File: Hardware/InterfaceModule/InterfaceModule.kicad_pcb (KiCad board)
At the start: 2 copper layers, 43 parts, among them J1 Selector Knob Connector, J10 External MIC IN, J11 TS-480 DATA, J12 D-700 DATA, J13 SignaLink 2 RADIO, J14 SignaLink 1 RADIO, J15 D-700 COM, J16 TS-480 COM, J17 External COM, J2 KrakenSDR Relay Enable, J3 External GPS IN, J4 External GPS OUT, J5 D-700 GPS, J6 D-700 MIC, J7 TS-480 MIC, J8 D-700 EXT.SP 1, J9 TS-480 EXT.SP, K1 FINDER-40.52, K10 FINDER-40.52, K11 FINDER-40.52, K12 FINDER-40.52, K13 FINDER-40.52, K14 FINDER-40.52, K15 FINDER-40.52, K16 FINDER-40.52, K17 FINDER-40.52, K18 FINDER-40.52, K19 FINDER-40.52, K2 FINDER-40.52, K20 FINDER-40.52, K21 FINDER-40.52, K22 FINDER-40.52, K3 FINDER-40.52, K4 FINDER-40.52, K5 FINDER-40.52, K6 FINDER-40.52, K7 FINDER-40.52, K8 FINDER-40.52, K9 FINDER-40.52

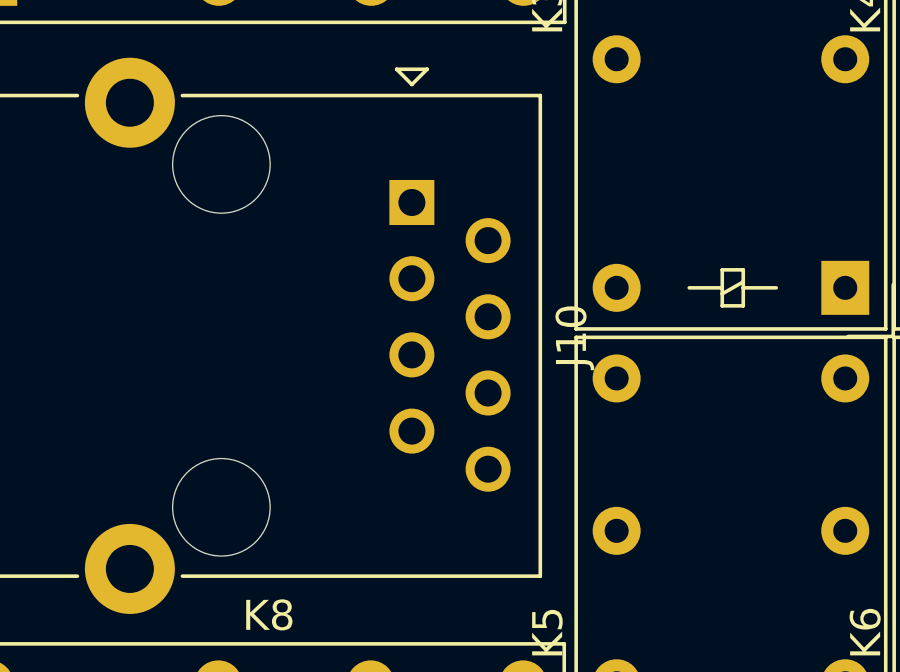
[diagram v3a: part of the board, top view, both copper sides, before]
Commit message: Added backplane between boards, redesigned selector
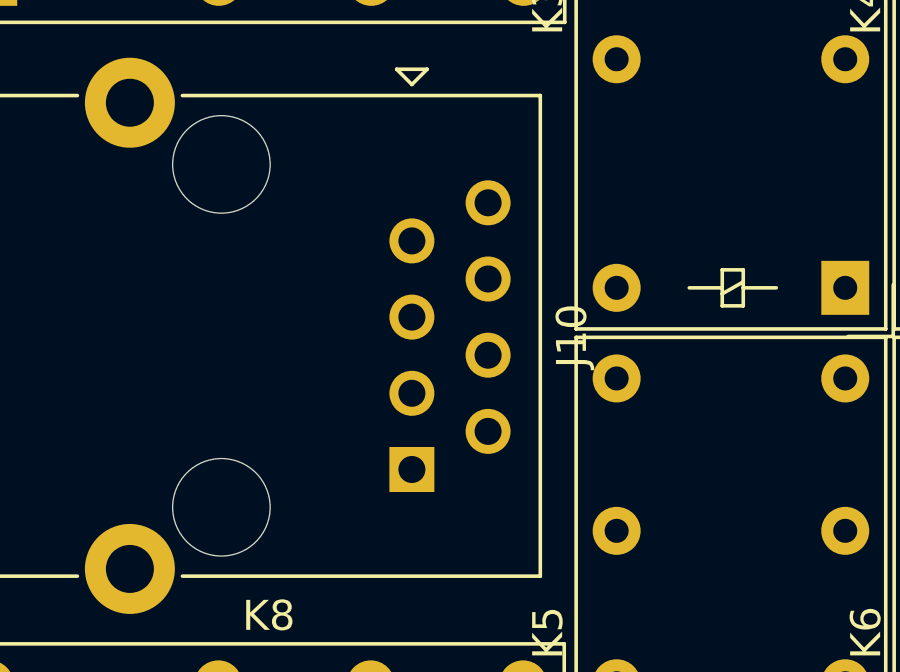
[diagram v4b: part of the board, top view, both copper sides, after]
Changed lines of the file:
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@@
     (pad "" np_thru_hole circle (at -1.27 6.35 270) (size 3.25 3.25) (drill 3.25) (layers *.Cu *.Mask))
     (pad "" np_thru_hole circle (at 10.16 6.35 90) (size 3.25 3.25) (drill 3.25) (layers *.Cu *.Mask))
-    (pad "1" thru_hole rect (at 0 0 90) (size 1.5 1.5) (drill 0.9) (layers *.Cu *.Mask)
+    (pad "1" thru_hole rect (at 8.9 0 90) (size 1.5 1.5) (drill 0.9) (layers *.Cu *.Mask)
       (net 22 "/Microphone Switching/EXT_UP") (pintype "passive"))
-    (pad "2" thru_hole circle (at 1.27 -2.54 90) (size 1.5 1.5) (drill 0.9) (layers *.Cu *.Mask)
+    (pad "2" thru_hole circle (at 7.63 -2.54 90) (size 1.5 1.5) (drill 0.9) (layers *.Cu *.Mask)
       (net 28 "/Microphone Switching/EXT_8V") (pintype "passive"))
-    (pad "3" thru_hole circle (at 2.54 0 90) (size 1.5 1.5) (drill 0.9) (layers *.Cu *.Mask)
+    (pad "3" thru_hole circle (at 6.36 0 90) (size 1.5 1.5) (drill 0.9) (layers *.Cu *.Mask)
       (net 29 "/Microphone Switching/EXT_GND") (pintype "passive"))
-    (pad "4" thru_hole circle (at 3.81 -2.54 90) (size 1.5 1.5) (drill 0.9) (layers *.Cu *.Mask)
+    (pad "4" thru_hole circle (at 5.09 -2.54 90) (size 1.5 1.5) (drill 0.9) (layers *.Cu *.Mask)
       (net 30 "/Microphone Switching/EXT_PTT") (pintype "passive"))
-    (pad "5" thru_hole circle (at 5.08 0 90) (size 1.5 1.5) (drill 0.9) (layers *.Cu *.Mask)
+    (pad "5" thru_hole circle (at 3.82 0 90) (size 1.5 1.5) (drill 0.9) (layers *.Cu *.Mask)
       (net 31 "/Microphone Switching/EXT_MICGND") (pintype "passive"))
-    (pad "6" thru_hole circle (at 6.35 -2.54 90) (size 1.5 1.5) (drill 0.9) (layers *.Cu *.Mask)
+    (pad "6" thru_hole circle (at 2.55 -2.54 90) (size 1.5 1.5) (drill 0.9) (layers *.Cu *.Mask)
       (net 33 "/Microphone Switching/EXT_MIC") (pintype "passive"))
-    (pad "7" thru_hole circle (at 7.62 0 90) (size 1.5 1.5) (drill 0.9) (layers *.Cu *.Mask)
+    (pad "7" thru_hole circle (at 1.28 0 90) (size 1.5 1.5) (drill 0.9) (layers *.Cu *.Mask)
       (net 34 "/Microphone Switching/EXT_NC") (pintype "passive"))
-    (pad "8" thru_hole circle (at 8.89 -2.54 90) (size 1.5 1.5) (drill 0.9) (layers *.Cu *.Mask)
+    (pad "8" thru_hole circle (at 0.01 -2.54 90) (size 1.5 1.5) (drill 0.9) (layers *.Cu *.Mask)
       (net 35 "/Microphone Switching/EXT_DWN") (pintype "passive"))
     (pad "SH" thru_hole circle (at -3.325 9.4 270) (size 3 3) (drill 1.6) (layers *.Cu *.Mask)

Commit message: Initial routings of data and main boards
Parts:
- removed J1: Selector Knob Connector, Connector_RJ:RJ45_Ninigi_GE
- removed J10: External MIC IN, Connector_RJ:RJ45_Ninigi_GE
- removed J11: TS-480 DATA, libraries:Connector_Mini-DIN_Female_6Pin_2rows
- removed J12: D-700 DATA, libraries:Connector_Mini-DIN_Female_6Pin_2rows
- removed J13: SignaLink 2 RADIO, Connector_RJ:RJ45_Ninigi_GE
- removed J14: SignaLink 1 RADIO, Connector_RJ:RJ45_Ninigi_GE
- removed J15: D-700 COM, Connector_Dsub:DSUB-9_Male_Horizontal_P2.77x2.84mm_EdgePinOffset7.70mm_Housed_MountingHolesOffset9.12mm
- removed J16: TS-480 COM, Connector_Dsub:DSUB-9_Male_Horizontal_P2.77x2.84mm_EdgePinOffset7.70mm_Housed_MountingHolesOffset9.12mm
- removed J17: External COM, Connector_Dsub:DSUB-9_Male_Horizontal_P2.77x2.84mm_EdgePinOffset7.70mm_Housed_MountingHolesOffset9.12mm
- removed J2: KrakenSDR Relay Enable, TerminalBlock_Phoenix:TerminalBlock_Phoenix_MKDS-1,5-2_1x02_P5.00mm_Horizontal
- removed J3: External GPS IN, Connector_Dsub:DSUB-9_Male_Horizontal_P2.77x2.84mm_EdgePinOffset7.70mm_Housed_MountingHolesOffset9.12mm
- removed J4: External GPS OUT, Connector_Dsub:DSUB-9_Male_Horizontal_P2.77x2.84mm_EdgePinOffset7.70mm_Housed_MountingHolesOffset9.12mm
- removed J5: D-700 GPS, libraries:Mystery_3.5mm
- removed J6: D-700 MIC, Connector_RJ:RJ45_Ninigi_GE
- removed J7: TS-480 MIC, Connector_RJ:RJ45_Ninigi_GE
- removed J8: D-700 EXT.SP 1, libraries:Mystery_3.5mm
- removed J9: TS-480 EXT.SP, libraries:Mystery_3.5mm
- removed K1, K10, K11, K12, K13, K14, K15, K16, K17, K18, K19, K2, K20, K21, K22, K3, K4, K5, K6, K7, K8, K9: FINDER-40.52, Relay_THT:Relay_DPDT_Finder_30.22
- removed R1, R2: 3.9Ohm, Resistor_THT:R_Axial_DIN0204_L3.6mm_D1.6mm_P2.54mm_Vertical
- removed R3, R4: 470Ohm, Resistor_THT:R_Axial_DIN0204_L3.6mm_D1.6mm_P2.54mm_Vertical
- added F101: 1A Trip, Fuse:Fuse_Bourns_MF-RG300, F.Cu at (-260.0, 69.0)
- added H101: Mounting Hole, libraries:M3_Mounting, F.Cu at (-274.0, 7.24)
- added H102: Mounting Hole, libraries:M3_Mounting, F.Cu at (-191.0, 7.24)
- added H103: Mounting Hole, libraries:M3_Mounting, F.Cu at (-191.0, 90.2)
- added H104: Mounting Hole, libraries:M3_Mounting, F.Cu at (-274.0, 90.2)
- added H201: Mounting Hole, libraries:M3_Mounting, F.Cu at (-112.0, 89.7)
- added H202: Mounting Hole, libraries:M3_Mounting, F.Cu at (-29.0, 6.74)
- added H203: Mounting Hole, libraries:M3_Mounting, F.Cu at (-112.0, 6.74)
- added H204: Mounting Hole, libraries:M3_Mounting, F.Cu at (-29.0, 89.7)
- added H301: Mounting Hole, libraries:M3_Mounting, F.Cu at (-200.0, 171.2)
- added H302: Mounting Hole, libraries:M3_Mounting, F.Cu at (-200.0, 254.2)
- added H303: Mounting Hole, libraries:M3_Mounting, F.Cu at (-283.0, 171.2)
- added H304: Mounting Hole, libraries:M3_Mounting, F.Cu at (-283.0, 254.2)
- added H401: Mounting Hole, libraries:M3_Mounting, F.Cu at (-29.0, 253.5)
- added H402: Mounting Hole, libraries:M3_Mounting, F.Cu at (-112.0, 170.5)
- added H403: Mounting Hole, libraries:M3_Mounting, F.Cu at (-112.0, 253.5)
- added H404: Mounting Hole, libraries:M3_Mounting, F.Cu at (-29.0, 170.5)
- added J101: Out 1 Header Debug Holes, libraries:2x07_Debug_Holes, F.Cu at (-255.3, 27.3)
- added J102: 2x05 IDC Header - OUT 1, Connector_IDC:IDC-Header_2x05_P2.54mm_Vertical, F.Cu at (-221.3, 9.99)
- added J103: Selector Knob Connector, libraries:Mystery_RJ45, F.Cu at (-262.5, 38.0)
- added J104: External Relay Enable, TerminalBlock_Phoenix:TerminalBlock_Phoenix_MKDS-1,5-2_1x02_P5.00mm_Horizontal, F.Cu at (-192.6, 65.8)
- added J105: Out 2 Header Debug Holes, libraries:2x07_Debug_Holes, F.Cu at (-257.6, 19.0)
- added J106: Debug Jumper Holes, libraries:2x07_Debug_Holes, F.Cu at (-225.6, 19.2)
- added J107: KrakenSDR Relay Enable, TerminalBlock_Phoenix:TerminalBlock_Phoenix_MKDS-1,5-2_1x02_P5.00mm_Horizontal, F.Cu at (-192.6, 36.8)
- added J108: 2x05 IDC Header - OUT 2, Connector_IDC:IDC-Header_2x05_P2.54mm_Vertical, F.Cu at (-253.8, 9.99)
- added J109: External GPS IN, Connector_Dsub:DSUB-9_Male_Horizontal_P2.77x2.84mm_EdgePinOffset7.70mm_Housed_MountingHolesOffset9.12mm, F.Cu at (-256.1, 82.9)
- added J110: External GPS OUT, Connector_Dsub:DSUB-9_Male_Horizontal_P2.77x2.84mm_EdgePinOffset7.70mm_Housed_MountingHolesOffset9.12mm, F.Cu at (-220.1, 82.9)
- added J111: D-700 GPS, libraries:Mystery_3.5mm, F.Cu at (-272.1, 53.0)
- added J112: Power IN, TerminalBlock_Phoenix:TerminalBlock_Phoenix_MKDS-1,5-2_1x02_P5.00mm_Horizontal, F.Cu at (-272.3, 69.1)
- added J201: D-700 MIC, libraries:Mystery_RJ45, F.Cu at (-100.5, 39.4)
- added J202: TS-480 MIC, libraries:Mystery_RJ45, F.Cu at (-100.5, 78.4)
- added J203: Out Header Debug Holes, libraries:2x07_Debug_Holes, F.Cu at (-92.1, 18.5)
- added J204: D-700 EXT.SP 1, libraries:Mystery_3.5mm, F.Cu at (-110.1, 16.7)
- added J205: In Header Debug Holes, libraries:2x07_Debug_Holes, F.Cu at (-60.0, 18.3)
- added J206: D-700 EXT.SP Passthrough, libraries:Mystery_3.5mm, F.Cu at (-45.6, 87.7)
- added J207: TS-480 EXT.SP, libraries:Mystery_3.5mm, F.Cu at (-110.1, 54.0)
- added J208: TS-480 EXT.SP Passthrough, libraries:Mystery_3.5mm, F.Cu at (-62.1, 87.7)
- added J209: External MIC IN, libraries:Mystery_RJ45, F.Cu at (-81.8, 77.8)
- added J210: 2x05 IDC Header - IN, Connector_IDC:IDC-Header_2x05_P2.54mm_Vertical, F.Cu at (-57.5, 9.51)
- added J211: 2x05 IDC Header - OUT, Connector_IDC:IDC-Header_2x05_P2.54mm_Vertical, F.Cu at (-91.8, 9.49)
- added J301: TS-480 DATA, libraries:Connector_Mini-DIN_Female_6Pin_2rows, F.Cu at (-277.5, 229.6)
- added J302: D-700 DATA, libraries:Connector_Mini-DIN_Female_6Pin_2rows, F.Cu at (-277.5, 198.5)
- added J303: SignaLink 2 RADIO, libraries:Mystery_RJ45, F.Cu at (-211.5, 225.5)
- added J304: SignaLink 1 RADIO, libraries:Mystery_RJ45, F.Cu at (-211.5, 193.6)
- added J305: Out Header Debug Holes, libraries:2x07_Debug_Holes, F.Cu at (-234.4, 183.0)
- added J306: In Header Debug Holes, libraries:2x07_Debug_Holes, F.Cu at (-266.8, 183.0)
- added J307: 2x05 IDC Header - IN, Connector_IDC:IDC-Header_2x05_P2.54mm_Vertical, F.Cu at (-262.8, 174.0)
- added J308: 2x05 IDC Header - OUT, Connector_IDC:IDC-Header_2x05_P2.54mm_Vertical, F.Cu at (-230.3, 174.0)
- added J401: D-700 COM, Connector_Dsub:DSUB-9_Male_Horizontal_P2.77x2.84mm_EdgePinOffset7.70mm_Housed_MountingHolesOffset9.12mm, F.Cu at (-104.7, 188.4)
- added J402: TS-480 COM, Connector_Dsub:DSUB-9_Male_Horizontal_P2.77x2.84mm_EdgePinOffset7.70mm_Housed_MountingHolesOffset9.12mm, F.Cu at (-104.7, 224.4)
- added J403: Out Header Debug Holes, libraries:2x07_Debug_Holes, F.Cu at (-94.4, 182.3)
- added J404: In Header Debug Holes, libraries:2x07_Debug_Holes, F.Cu at (-61.9, 182.3)
- added J405: External COM, Connector_Dsub:DSUB-9_Male_Horizontal_P2.77x2.84mm_EdgePinOffset7.70mm_Housed_MountingHolesOffset9.12mm, F.Cu at (-76.0, 246.2)
- added J406: 2x05 IDC Header - IN, Connector_IDC:IDC-Header_2x05_P2.54mm_Vertical, F.Cu at (-59.3, 173.2)
- added J407: 2x05 IDC Header - OUT, Connector_IDC:IDC-Header_2x05_P2.54mm_Vertical, F.Cu at (-91.8, 173.2)
- added K201: FINDER-40.52, Relay_THT:Relay_DPDT_Finder_30.22, F.Cu at (-81.3, 40.4)
- added K202: FINDER-40.52, Relay_THT:Relay_DPDT_Finder_30.22, F.Cu at (-29.8, 45.8)
- added K203: FINDER-40.52, Relay_THT:Relay_DPDT_Finder_30.22, F.Cu at (-29.8, 68.1)
- added K204: FINDER-40.52, Relay_THT:Relay_DPDT_Finder_30.22, F.Cu at (-81.3, 64.0)
- added K205: FINDER-40.52, Relay_THT:Relay_DPDT_Finder_30.22, F.Cu at (-59.3, 40.4)
- added K206: FINDER-40.52, Relay_THT:Relay_DPDT_Finder_30.22, F.Cu at (-59.3, 52.2)
- added K207: FINDER-40.52, Relay_THT:Relay_DPDT_Finder_30.22, F.Cu at (-81.3, 52.2)
- added K208: FINDER-40.52, Relay_THT:Relay_DPDT_Finder_30.22, F.Cu at (-59.3, 64.0)
- added K301: FINDER-40.52, Relay_THT:Relay_DPDT_Finder_30.22, F.Cu at (-247.9, 235.6)
- added K302: FINDER-40.52, Relay_THT:Relay_DPDT_Finder_30.22, F.Cu at (-252.2, 231.2)
- added K303: FINDER-40.52, Relay_THT:Relay_DPDT_Finder_30.22, F.Cu at (-259.7, 235.6)
- added K304: FINDER-40.52, Relay_THT:Relay_DPDT_Finder_30.22, F.Cu at (-240.3, 231.2)
- added K305: FINDER-40.52, Relay_THT:Relay_DPDT_Finder_30.22, F.Cu at (-236.1, 235.6)
- added K306: FINDER-40.52, Relay_THT:Relay_DPDT_Finder_30.22, F.Cu at (-228.5, 231.2)
- added K401: FINDER-40.52, Relay_THT:Relay_DPDT_Finder_30.22, F.Cu at (-70.3, 199.5)
- added K402: FINDER-40.52, Relay_THT:Relay_DPDT_Finder_30.22, F.Cu at (-47.8, 199.5)
- added K403: FINDER-40.52, Relay_THT:Relay_DPDT_Finder_30.22, F.Cu at (-48.3, 235.5)
- added K404: FINDER-40.52, Relay_THT:Relay_DPDT_Finder_30.22, F.Cu at (-70.3, 223.5)
- added K405: FINDER-40.52, Relay_THT:Relay_DPDT_Finder_30.22, F.Cu at (-70.3, 211.5)
- added K406: FINDER-40.52, Relay_THT:Relay_DPDT_Finder_30.22, F.Cu at (-47.8, 223.5)
- added K407: FINDER-40.52, Relay_THT:Relay_DPDT_Finder_30.22, F.Cu at (-47.8, 211.5)
- added K408: FINDER-40.52, Relay_THT:Relay_DPDT_Finder_30.22, F.Cu at (-70.3, 235.5)
- added R201: 3.9Ohm, Resistor_THT:R_Axial_DIN0204_L3.6mm_D1.6mm_P2.54mm_Vertical, F.Cu at (-99.3, 22.7)
- added R202: 3.9Ohm, Resistor_THT:R_Axial_DIN0204_L3.6mm_D1.6mm_P2.54mm_Vertical, F.Cu at (-99.3, 60.0)
- added R203: 470Ohm, Resistor_THT:R_Axial_DIN0204_L3.6mm_D1.6mm_P2.54mm_Vertical, F.Cu at (-109.7, 22.7)
- added R204: 470Ohm, Resistor_THT:R_Axial_DIN0204_L3.6mm_D1.6mm_P2.54mm_Vertical, F.Cu at (-109.7, 60.0)
- added U101: 12V Variable Boost Buck Converter, libraries:BoostBuck, F.Cu at (-236.1, 74.8)
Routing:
- net /Data Port Switching/Knob_Pos_2: track 0.00 -> 207.2 mm
- net /Main & GPS Switching/Knob_Pos_6_Raw: track 0.00 -> 190.3 mm
- net /Data Port Switching/Knob_Pos_1: track 0.00 -> 163.2 mm
- net /Main & GPS Switching/Knob_Pos_7_Raw: track 0.00 -> 154.3 mm
- net /Main & GPS Switching/Knob_Pos_5_Raw: track 0.00 -> 110.0 mm
- net /Main & GPS Switching/Knob_Pos_1_Raw: track 0.00 -> 103.6 mm
- net /Main & GPS Switching/Knob_Pos_3_Raw: track 0.00 -> 101.9 mm
- net /Main & GPS Switching/Knob_Pos_2_Raw: track 0.00 -> 101.8 mm
- net /Main & GPS Switching/Knob_Pos_4_Raw: track 0.00 -> 101.6 mm
- net +12P: track 0.00 -> 77.4 mm
- net Net-(J109-Pad2): track 0.00 -> 77.3 mm
- net GND: track 0.00 -> 67.6 mm
- net /Data Port Switching/SignaLink2_RADIO_5: track 0.00 -> 65.3 mm
- net /Data Port Switching/SignaLink2_RADIO_1: track 0.00 -> 63.0 mm
- net /Data Port Switching/D700_DATA_PKD: track 0.00 -> 59.9 mm
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- added copper zone on F.Cu, net +12P
- added copper zone on B.Cu, net GND
- added copper zone on F.Cu, net GND
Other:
- board outline added: 261 x 254.5 mm

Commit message: Routed mic board
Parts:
- removed J101: Out 1 Header Debug Holes, libraries:2x07_Debug_Holes
- removed J105: Out 2 Header Debug Holes, libraries:2x07_Debug_Holes
- removed J106: Debug Jumper Holes, libraries:2x07_Debug_Holes
- removed J203: Out Header Debug Holes, libraries:2x07_Debug_Holes
- removed J205: In Header Debug Holes, libraries:2x07_Debug_Holes
- added D101: D_Small_Filled, Diode_THT:D_A-405_P2.54mm_Vertical_AnodeUp, F.Cu at (-253.3, 26.7)
- added D102: D_Small_Filled, Diode_THT:D_A-405_P2.54mm_Vertical_AnodeUp, F.Cu at (-253.3, 29.9)
- added D103: D_Small_Filled, Diode_THT:D_A-405_P2.54mm_Vertical_AnodeUp, F.Cu at (-253.3, 33.1)
- added D104: D_Small_Filled, Diode_THT:D_A-405_P2.54mm_Vertical_AnodeUp, F.Cu at (-253.3, 36.2)
- added D105: D_Small_Filled, Diode_THT:D_A-405_P2.54mm_Vertical_AnodeUp, F.Cu at (-253.3, 39.4)
- added D106: D_Small_Filled, Diode_THT:D_A-405_P2.54mm_Vertical_AnodeUp, F.Cu at (-253.3, 42.6)
- added D107: D_Small_Filled, Diode_THT:D_A-405_P2.54mm_Vertical_AnodeUp, F.Cu at (-253.3, 45.8)
- added D201: D_Small_Filled, Diode_THT:D_A-405_P2.54mm_Vertical_AnodeUp, F.Cu at (-79.9, 20.0)
- added D202: D_Small_Filled, Diode_THT:D_A-405_P2.54mm_Vertical_AnodeUp, F.Cu at (-76.6, 20.0)
- added D203: D_Small_Filled, Diode_THT:D_A-405_P2.54mm_Vertical_AnodeUp, F.Cu at (-73.3, 20.0)
- added D204: D_Small_Filled, Diode_THT:D_A-405_P2.54mm_Vertical_AnodeUp, F.Cu at (-70.0, 20.0)
- added D205: D_Small_Filled, Diode_THT:D_A-405_P2.54mm_Vertical_AnodeUp, F.Cu at (-66.7, 20.0)
- added D206: D_Small_Filled, Diode_THT:D_A-405_P2.54mm_Vertical_AnodeUp, F.Cu at (-63.4, 20.0)
- added D207: D_Small_Filled, Diode_THT:D_A-405_P2.54mm_Vertical_AnodeUp, F.Cu at (-60.1, 20.0)
- added D208: D_Small_Filled, Diode_THT:D_A-405_P2.54mm_Vertical_AnodeUp, F.Cu at (-82.5, 23.8)
- added D209: D_Small_Filled, Diode_THT:D_A-405_P2.54mm_Vertical_AnodeUp, F.Cu at (-75.8, 23.8)
- added D210: D_Small_Filled, Diode_THT:D_A-405_P2.54mm_Vertical_AnodeUp, F.Cu at (-67.5, 23.8)
- added D211: D_Small_Filled, Diode_THT:D_A-405_P2.54mm_Vertical_AnodeUp, F.Cu at (-61.7, 23.8)
- added D301: D_Small_Filled, Diode_THT:D_A-405_P2.54mm_Vertical_AnodeUp, F.Cu at (-319.1, 200.9)
- added D302: D_Small_Filled, Diode_THT:D_A-405_P2.54mm_Vertical_AnodeUp, F.Cu at (-319.1, 192.4)
- added D303: D_Small_Filled, Diode_THT:D_A-405_P2.54mm_Vertical_AnodeUp, F.Cu at (-312.7, 196.7)
- added D304: D_Small_Filled, Diode_THT:D_A-405_P2.54mm_Vertical_AnodeUp, F.Cu at (-300.0, 188.2)
- added D305: D_Small_Filled, Diode_THT:D_A-405_P2.54mm_Vertical_AnodeUp, F.Cu at (-312.7, 188.2)
- added D306: D_Small_Filled, Diode_THT:D_A-405_P2.54mm_Vertical_AnodeUp, F.Cu at (-300.0, 192.4)
- added D307: D_Small_Filled, Diode_THT:D_A-405_P2.54mm_Vertical_AnodeUp, F.Cu at (-306.4, 188.2)
- added D308: D_Small_Filled, Diode_THT:D_A-405_P2.54mm_Vertical_AnodeUp, F.Cu at (-319.1, 188.2)
- added D309: D_Small_Filled, Diode_THT:D_A-405_P2.54mm_Vertical_AnodeUp, F.Cu at (-319.1, 196.7)
- added D310: D_Small_Filled, Diode_THT:D_A-405_P2.54mm_Vertical_AnodeUp, F.Cu at (-306.4, 192.4)
- added D311: D_Small_Filled, Diode_THT:D_A-405_P2.54mm_Vertical_AnodeUp, F.Cu at (-306.4, 200.9)
- added D312: D_Small_Filled, Diode_THT:D_A-405_P2.54mm_Vertical_AnodeUp, F.Cu at (-312.7, 200.9)
- added D313: D_Small_Filled, Diode_THT:D_A-405_P2.54mm_Vertical_AnodeUp, F.Cu at (-312.7, 192.4)
- added D314: D_Small_Filled, Diode_THT:D_A-405_P2.54mm_Vertical_AnodeUp, F.Cu at (-306.4, 196.7)
- added D401: D_Small_Filled, Diode_THT:D_A-405_P2.54mm_Vertical_AnodeUp, F.Cu at (-8.95, 169.8)
- added D402: D_Small_Filled, Diode_THT:D_A-405_P2.54mm_Vertical_AnodeUp, F.Cu at (-2.60, 169.8)
- added D403: D_Small_Filled, Diode_THT:D_A-405_P2.54mm_Vertical_AnodeUp, F.Cu at (-2.60, 178.3)
- added D404: D_Small_Filled, Diode_THT:D_A-405_P2.54mm_Vertical_AnodeUp, F.Cu at (3.73, 174.1)
- added D405: D_Small_Filled, Diode_THT:D_A-405_P2.54mm_Vertical_AnodeUp, F.Cu at (-2.60, 182.6)
- added D406: D_Small_Filled, Diode_THT:D_A-405_P2.54mm_Vertical_AnodeUp, F.Cu at (-15.3, 178.3)
- added D407: D_Small_Filled, Diode_THT:D_A-405_P2.54mm_Vertical_AnodeUp, F.Cu at (-8.95, 178.3)
- added D408: D_Small_Filled, Diode_THT:D_A-405_P2.54mm_Vertical_AnodeUp, F.Cu at (3.73, 169.8)
- added D409: D_Small_Filled, Diode_THT:D_A-405_P2.54mm_Vertical_AnodeUp, F.Cu at (-15.3, 182.6)
- added D410: D_Small_Filled, Diode_THT:D_A-405_P2.54mm_Vertical_AnodeUp, F.Cu at (-8.95, 174.1)
- added D411: D_Small_Filled, Diode_THT:D_A-405_P2.54mm_Vertical_AnodeUp, F.Cu at (-15.3, 174.1)
- added D412: D_Small_Filled, Diode_THT:D_A-405_P2.54mm_Vertical_AnodeUp, F.Cu at (-15.3, 169.8)
- added D413: D_Small_Filled, Diode_THT:D_A-405_P2.54mm_Vertical_AnodeUp, F.Cu at (-2.60, 174.1)
- added D414: D_Small_Filled, Diode_THT:D_A-405_P2.54mm_Vertical_AnodeUp, F.Cu at (-8.95, 182.6)
- moved K401 47.0 mm to (-94.4, 239.8)
- moved K205 41.6 mm to (-88.8, 69.7)
- moved K208 39.8 mm to (-38.5, 30.2), turned to -90 degrees
- moved K406 36.9 mm to (-61.5, 189.2), turned to -90 degrees
- moved K203 36.1 mm to (-63.3, 54.7), turned to 0 degrees
- moved K404 35.3 mm to (-94.4, 197.6)
- moved K201 34.4 mm to (-63.3, 69.7)
- moved K408 33.9 mm to (-94.4, 211.7)
- moved K202 33.7 mm to (-63.0, 40.0), turned to 0 degrees
- moved J209 33.5 mm to (-48.3, 77.8)
- moved K405 28.0 mm to (-94.4, 225.8)
- moved J206 27.4 mm to (-73.0, 87.7)
- moved J208 27.4 mm to (-89.5, 87.7)
- moved K204 25.4 mm to (-88.8, 39.7)
- moved K206 20.9 mm to (-38.5, 53.8), turned to -90 degrees
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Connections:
- net /COM Port Switching/Knob_Pos_3 renamed /COM Port Switching/Knob_Pos_3_Raw
- net /COM Port Switching/Knob_Pos_4 renamed /COM Port Switching/Knob_Pos_4_Raw
- net /COM Port Switching/Knob_Pos_5 renamed /COM Port Switching/Knob_Pos_5_Raw
- net /COM Port Switching/Knob_Pos_6 renamed /COM Port Switching/Knob_Pos_6_Raw
- net /COM Port Switching/Knob_Pos_7 renamed /COM Port Switching/Knob_Pos_7_Raw
- net /Data Port Switching/Knob_Pos_3 renamed /Data Port Switching/Knob_Pos_3_Raw
- net /Data Port Switching/Knob_Pos_4 renamed /Data Port Switching/Knob_Pos_4_Raw
- net /Data Port Switching/Knob_Pos_5 renamed /Data Port Switching/Knob_Pos_5_Raw
- net /Data Port Switching/Knob_Pos_6 renamed /Data Port Switching/Knob_Pos_6_Raw
- net /Data Port Switching/Knob_Pos_7 renamed /Data Port Switching/Knob_Pos_7_Raw
- net /Microphone Switching/Knob_Pos_2 renamed /Microphone Switching/Knob_Pos_2_Raw
- net /Microphone Switching/Knob_Pos_6 renamed /Microphone Switching/Knob_Pos_6_Raw
- net /Microphone Switching/Knob_Pos_7 renamed /Microphone Switching/Knob_Pos_7_Raw
- J102 pad 2: /Main & GPS Switching/Knob_Pos_5_Raw -> /Main & GPS Switching/Knob_Pos_5
- J102 pad 3: /Main & GPS Switching/Knob_Pos_1_Raw -> /Main & GPS Switching/Knob_Pos_1
- J102 pad 4: /Main & GPS Switching/Knob_Pos_6_Raw -> /Main & GPS Switching/Knob_Pos_6
- J102 pad 5: /Main & GPS Switching/Knob_Pos_2_Raw -> /Main & GPS Switching/Knob_Pos_2
- J102 pad 6: /Main & GPS Switching/Knob_Pos_7_Raw -> /Main & GPS Switching/Knob_Pos_7
- J102 pad 7: /Main & GPS Switching/Knob_Pos_3_Raw -> /Main & GPS Switching/Knob_Pos_3
- J102 pad 9: /Main & GPS Switching/Knob_Pos_4_Raw -> /Main & GPS Switching/Knob_Pos_4
- J103 pad 2: /Main & GPS Switching/Knob_Pos_1_Raw -> Net-(J103-Pad2)
- J103 pad 3: /Main & GPS Switching/Knob_Pos_2_Raw -> Net-(J103-Pad3)
- J103 pad 4: /Main & GPS Switching/Knob_Pos_3_Raw -> Net-(J103-Pad4)
- J103 pad 5: /Main & GPS Switching/Knob_Pos_4_Raw -> Net-(J103-Pad5)
- J103 pad 6: /Main & GPS Switching/Knob_Pos_5_Raw -> Net-(J103-Pad6)
- J103 pad 7: /Main & GPS Switching/Knob_Pos_6_Raw -> Net-(J103-Pad7)
- J103 pad 8: /Main & GPS Switching/Knob_Pos_7_Raw -> Net-(J103-Pad8)
- J104 pad 1: /Main & GPS Switching/Knob_Pos_6_Raw -> /Main & GPS Switching/Knob_Pos_6
- J107 pad 1: /Main & GPS Switching/Knob_Pos_7_Raw -> /Main & GPS Switching/Knob_Pos_7
- J108 pad 2: /Main & GPS Switching/Knob_Pos_5_Raw -> /Main & GPS Switching/Knob_Pos_5
- J108 pad 3: /Main & GPS Switching/Knob_Pos_1_Raw -> /Main & GPS Switching/Knob_Pos_1
- J108 pad 4: /Main & GPS Switching/Knob_Pos_6_Raw -> /Main & GPS Switching/Knob_Pos_6
- J108 pad 5: /Main & GPS Switching/Knob_Pos_2_Raw -> /Main & GPS Switching/Knob_Pos_2
- J108 pad 6: /Main & GPS Switching/Knob_Pos_7_Raw -> /Main & GPS Switching/Knob_Pos_7
- J108 pad 7: /Main & GPS Switching/Knob_Pos_3_Raw -> /Main & GPS Switching/Knob_Pos_3
- J108 pad 9: /Main & GPS Switching/Knob_Pos_4_Raw -> /Main & GPS Switching/Knob_Pos_4
- J210 pad 2: /Microphone Switching/Knob_Pos_1 -> /Microphone Switching/Knob_Pos_5_Raw
- J210 pad 3: /Microphone Switching/Knob_Pos_1 -> /Microphone Switching/Knob_Pos_1_Raw
- J210 pad 7: /Microphone Switching/Knob_Pos_1 -> /Microphone Switching/Knob_Pos_3_Raw
- J210 pad 9: /Microphone Switching/Knob_Pos_1 -> /Microphone Switching/Knob_Pos_4_Raw
- J211 pad 2: /Microphone Switching/Knob_Pos_1 -> /Microphone Switching/Knob_Pos_5_Raw
- J211 pad 3: /Microphone Switching/Knob_Pos_1 -> /Microphone Switching/Knob_Pos_1_Raw
- J211 pad 7: /Microphone Switching/Knob_Pos_1 -> /Microphone Switching/Knob_Pos_3_Raw
- J211 pad 9: /Microphone Switching/Knob_Pos_1 -> /Microphone Switching/Knob_Pos_4_Raw
- J305 pad 1a: /Data Port Switching/Knob_Pos_1 -> /Data Port Switching/Knob_Pos_1_Raw
- J305 pad 1b: /Data Port Switching/Knob_Pos_1 -> /Data Port Switching/Knob_Pos_1_Raw
- J305 pad 2a: /Data Port Switching/Knob_Pos_2 -> /Data Port Switching/Knob_Pos_2_Raw
- J305 pad 2b: /Data Port Switching/Knob_Pos_2 -> /Data Port Switching/Knob_Pos_2_Raw
- J306 pad 1a: /Data Port Switching/Knob_Pos_1 -> /Data Port Switching/Knob_Pos_1_Raw
- J306 pad 1b: /Data Port Switching/Knob_Pos_1 -> /Data Port Switching/Knob_Pos_1_Raw
- J306 pad 2a: /Data Port Switching/Knob_Pos_2 -> /Data Port Switching/Knob_Pos_2_Raw
- J306 pad 2b: /Data Port Switching/Knob_Pos_2 -> /Data Port Switching/Knob_Pos_2_Raw
- J307 pad 3: /Data Port Switching/Knob_Pos_1 -> /Data Port Switching/Knob_Pos_1_Raw
- J307 pad 5: /Data Port Switching/Knob_Pos_2 -> /Data Port Switching/Knob_Pos_2_Raw
- J308 pad 3: /Data Port Switching/Knob_Pos_1 -> /Data Port Switching/Knob_Pos_1_Raw
- J308 pad 5: /Data Port Switching/Knob_Pos_2 -> /Data Port Switching/Knob_Pos_2_Raw
- J403 pad 1a: /COM Port Switching/Knob_Pos_1 -> /COM Port Switching/Knob_Pos_1_Raw
- J403 pad 1b: /COM Port Switching/Knob_Pos_1 -> /COM Port Switching/Knob_Pos_1_Raw
- J403 pad 2a: /COM Port Switching/Knob_Pos_2 -> /COM Port Switching/Knob_Pos_2_Raw
- J403 pad 2b: /COM Port Switching/Knob_Pos_2 -> /COM Port Switching/Knob_Pos_2_Raw
- J404 pad 1a: /COM Port Switching/Knob_Pos_1 -> /COM Port Switching/Knob_Pos_1_Raw
- J404 pad 1b: /COM Port Switching/Knob_Pos_1 -> /COM Port Switching/Knob_Pos_1_Raw
- J404 pad 2a: /COM Port Switching/Knob_Pos_2 -> /COM Port Switching/Knob_Pos_2_Raw
- J404 pad 2b: /COM Port Switching/Knob_Pos_2 -> /COM Port Switching/Knob_Pos_2_Raw
- J406 pad 3: /COM Port Switching/Knob_Pos_1 -> /COM Port Switching/Knob_Pos_1_Raw
- J406 pad 5: /COM Port Switching/Knob_Pos_2 -> /COM Port Switching/Knob_Pos_2_Raw
- J407 pad 3: /COM Port Switching/Knob_Pos_1 -> /COM Port Switching/Knob_Pos_1_Raw
- J407 pad 5: /COM Port Switching/Knob_Pos_2 -> /COM Port Switching/Knob_Pos_2_Raw
- K202 pad 12: unconnected-(K202-Pad12) -> /Microphone Switching/EXT_8V
- K202 pad 14: /Microphone Switching/EXT_8V -> unconnected-(K202-Pad14)
- K202 pad 22: unconnected-(K202-Pad22) -> /Microphone Switching/EXT_UP
- K202 pad 24: /Microphone Switching/EXT_UP -> unconnected-(K202-Pad24)
- K202 pad A1: /Microphone Switching/Knob_Pos_1 -> /Microphone Switching/RightBank
- K204 pad 12: unconnected-(K204-Pad12) -> /Microphone Switching/EXT_PTT
- K204 pad 14: /Microphone Switching/EXT_PTT -> unconnected-(K204-Pad14)
- K204 pad 22: unconnected-(K204-Pad22) -> /Microphone Switching/EXT_GND
- K204 pad 24: /Microphone Switching/EXT_GND -> unconnected-(K204-Pad24)
- K204 pad A1: /Microphone Switching/Knob_Pos_1 -> /Microphone Switching/RightBank
- K205 pad 22: /Microphone Switching/D700_SP_T -> /Microphone Switching/D700_SP_S
- K206 pad 12: Net-(K206-Pad12) -> /Microphone Switching/EXT_MIC
- K206 pad 14: /Microphone Switching/EXT_MIC -> Net-(R202-Pad2)
- K206 pad 22: /Microphone Switching/480_SP_T -> /Microphone Switching/EXT_MICGND
- K206 pad 24: /Microphone Switching/EXT_MICGND -> /Microphone Switching/480_SP_S
- K206 pad A1: /Microphone Switching/Knob_Pos_1 -> /Microphone Switching/RightBank
- K208 pad 12: unconnected-(K208-Pad12) -> /Microphone Switching/EXT_DWN
- K208 pad 14: /Microphone Switching/EXT_DWN -> unconnected-(K208-Pad14)
- K208 pad 22: unconnected-(K208-Pad22) -> /Microphone Switching/EXT_NC
- K208 pad 24: /Microphone Switching/EXT_NC -> unconnected-(K208-Pad24)
- K208 pad A1: /Microphone Switching/Knob_Pos_1 -> /Microphone Switching/RightBank
- R201 pad 1: /Microphone Switching/D700_SP_T -> /Microphone Switching/D700_SP_S
- R202 pad 1: /Microphone Switching/480_SP_T -> /Microphone Switching/480_SP_S
- R202 pad 2: Net-(K206-Pad12) -> Net-(R202-Pad2)
- R203 pad 1: /Microphone Switching/D700_SP_S -> /Microphone Switching/D700_SP_T
- R204 pad 1: /Microphone Switching/480_SP_S -> /Microphone Switching/480_SP_T
- R204 pad 2: Net-(K206-Pad12) -> Net-(R202-Pad2)
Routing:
- net /Main & GPS Switching/Knob_Pos_6_Raw: track 190.3 -> 0.00 mm
- net /Main & GPS Switching/Knob_Pos_6: track 0.00 -> 170.3 mm, vias 0 -> 2
- net /Main & GPS Switching/Knob_Pos_7_Raw: track 154.3 -> 0.00 mm
- net /Microphone Switching/RightBank: track 0.00 -> 153.2 mm
- net /Main & GPS Switching/Knob_Pos_7: track 0.00 -> 148.1 mm, vias 0 -> 2
- net /Microphone Switching/Knob_Pos_1: track 0.00 -> 145.4 mm
- net Net-(R202-Pad2): track 0.00 -> 143.8 mm
- net /Data Port Switching/Knob_Pos_2: track 207.2 -> 85.1 mm
- net /Microphone Switching/480_SP_S: track 0.00 -> 114.9 mm
- net /Main & GPS Switching/Knob_Pos_5_Raw: track 110.0 -> 0.00 mm
- net /Microphone Switching/D700_MICGND: track 0.00 -> 107.8 mm
- net /Microphone Switching/D700_MIC: track 0.00 -> 105.7 mm
- net /Main & GPS Switching/Knob_Pos_5: track 0.00 -> 105.0 mm, vias 0 -> 2
- net /Main & GPS Switching/Knob_Pos_4: track 0.00 -> 104.1 mm, vias 0 -> 1
- net /Main & GPS Switching/Knob_Pos_1_Raw: track 103.6 -> 0.00 mm
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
